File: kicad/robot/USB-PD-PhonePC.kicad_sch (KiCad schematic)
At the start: 42 parts, among them IC1 TPS61253AYFFR, IC4 EFC4626R-TR, U11 MAX77958EWV+T, U15 ESD122DMYR

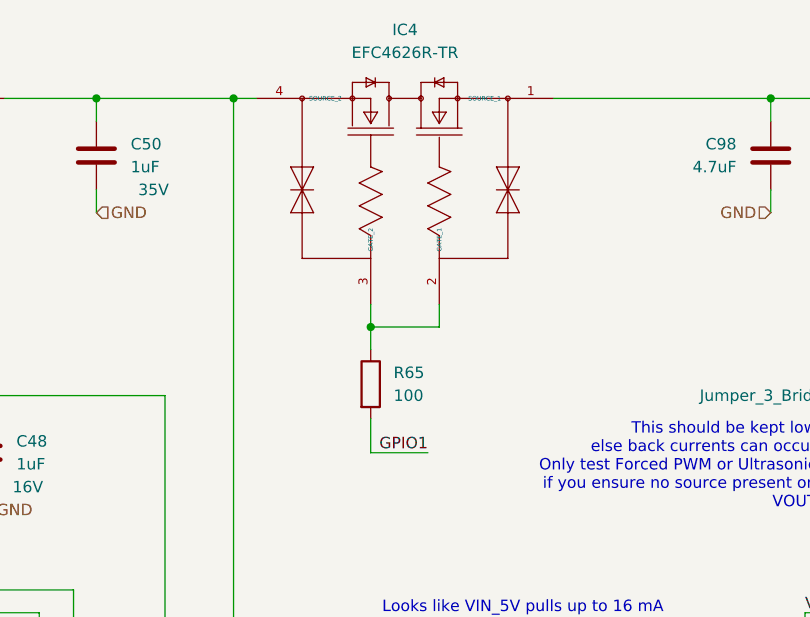
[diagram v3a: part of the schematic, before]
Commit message: Replaced dual mosfet with cheaper pair and common source.
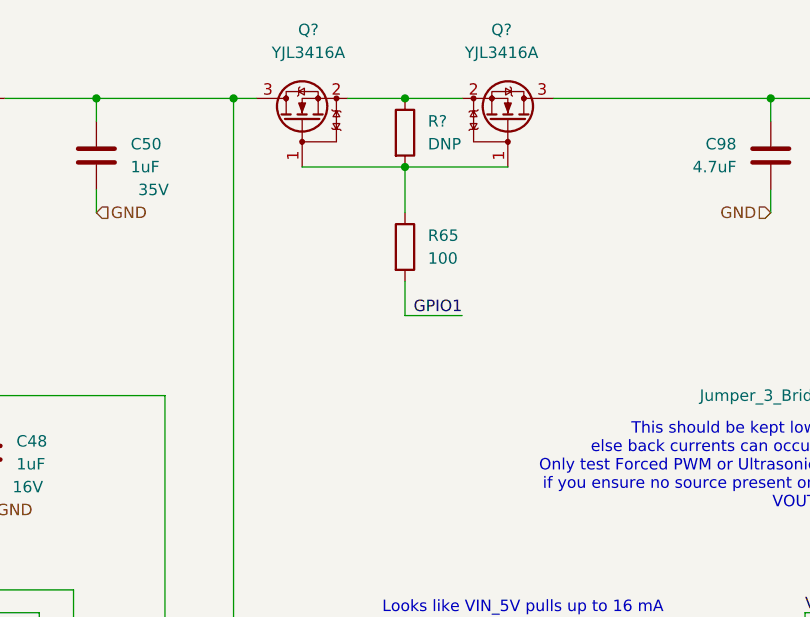
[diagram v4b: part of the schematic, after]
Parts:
- removed IC4: EFC4626R-TR, Package_BGA:ON_SEMI_EFCP1010-4DG-020, symbol Power_Management:EFC4626R-TR
- added Q? (x2): YJL3416A, Package_TO_SOT_SMD:SOT-23, symbol Transistor_FET:YJL3416A
- added R?: DNP, Resistor_SMD:R_0603_1608Metric, symbol Device:R
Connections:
- net at C100.1, C98.1, C99.1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: now also Q?.3 (D)
- net at R65.1: now also Q?.1 (G), Q?.1 (G), R?.2
- net at C50.1, JP4.2 (B), U11.A6 (VBUS): now also Q?.3 (D)
- new net: Q?.2 (S), Q?.2 (S), R?.1
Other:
- moved on the sheet: R65
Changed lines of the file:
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@@
   (junction (at 287.02 293.37) (diameter 0) (color 0 0 0 0)
   )
+  (junction (at 267.97 128.27) (diameter 0) (color 0 0 0 0)
+  )
   (junction (at 322.58 120.65) (diameter 0) (color 0 0 0 0)
   )
@@
   (junction (at 331.47 246.38) (diameter 0) (color 0 0 0 0)
   )
-  (junction (at 264.16 146.05) (diameter 0) (color 0 0 0 0)
-  )
   (junction (at 339.09 234.95) (diameter 0) (color 0 0 0 0)
   )
@@
   )
   (junction (at 236.22 267.97) (diameter 0) (color 0 0 0 0)
+  )
+  (junction (at 267.97 120.65) (diameter 0) (color 0 0 0 0)
   )
   (junction (at 187.96 201.93) (diameter 0) (color 0 0 0 0)
@@
     (stroke (width 0) (type default) (color 0 0 0 0))
   )
-  (wire (pts (xy 264.16 156.21) (xy 264.16 160.02))
+  (wire (pts (xy 267.97 140.97) (xy 267.97 144.78))
     (stroke (width 0) (type default) (color 0 0 0 0))
   )
@@
     (stroke (width 0) (type default) (color 0 0 0 0))
   )
-  (wire (pts (xy 264.16 160.02) (xy 270.51 160.02))
+  (wire (pts (xy 267.97 144.78) (xy 274.32 144.78))
     (stroke (width 0) (type default) (color 0 0 0 0))
   )
@@
     (stroke (width 0) (type default) (color 0 0 0 0))
   )
+  (wire (pts (xy 261.62 120.65) (xy 267.97 120.65))
+    (stroke (width 0) (type default) (color 0 0 0 0))
+  )
   (wire (pts (xy 309.88 254) (xy 316.23 254))
     (stroke (width 0) (type default) (color 0 0 0 0))
@@
     (stroke (width 0) (type default) (color 0 0 0 0))
   )
-  (wire (pts (xy 271.78 143.51) (xy 271.78 146.05))
-    (stroke (width 0) (type default) (color 0 0 0 0))
-  )
   (wire (pts (xy 227.33 215.9) (xy 264.16 215.9))
     (stroke (width 0) (type default) (color 0 0 0 0))
@@
     (stroke (width 0) (type default) (color 0 0 0 0))
   )
-  (wire (pts (xy 264.16 146.05) (xy 264.16 143.51))
+  (wire (pts (xy 267.97 128.27) (xy 267.97 133.35))
     (stroke (width 0) (type default) (color 0 0 0 0))
   )
@@
     (stroke (width 0) (type default) (color 0 0 0 0))
   )
+  (wire (pts (xy 256.54 128.27) (xy 267.97 128.27))
+    (stroke (width 0) (type default) (color 0 0 0 0))
+  )
   (wire (pts (xy 379.73 120.65) (xy 375.92 120.65))
     (stroke (width 0) (type default) (color 0 0 0 0))
@@
     (stroke (width 0) (type default) (color 0 0 0 0))
   )
-  (wire (pts (xy 264.16 148.59) (xy 264.16 146.05))
-    (stroke (width 0) (type default) (color 0 0 0 0))
-  )
   (wire (pts (xy 339.09 269.24) (xy 339.09 264.16))
     (stroke (width 0) (type default) (color 0 0 0 0))
@@
     (stroke (width 0) (type default) (color 0 0 0 0))
   )
-  (wire (pts (xy 271.78 146.05) (xy 264.16 146.05))
-    (stroke (width 0) (type default) (color 0 0 0 0))
-  )
   (wire (pts (xy 309.88 218.44) (xy 317.5 218.44))
     (stroke (width 0) (type default) (color 0 0 0 0))
@@
     (stroke (width 0) (type default) (color 0 0 0 0))
   )
+  (wire (pts (xy 267.97 128.27) (xy 279.4 128.27))
+    (stroke (width 0) (type default) (color 0 0 0 0))
+  )
   (wire (pts (xy 200.66 120.65) (xy 213.36 120.65))
     (stroke (width 0) (type default) (color 0 0 0 0))
@@
   )
   (wire (pts (xy 242.57 267.97) (xy 236.22 267.97))
+    (stroke (width 0) (type default) (color 0 0 0 0))
+  )
+  (wire (pts (xy 267.97 120.65) (xy 274.32 120.65))
     (stroke (width 0) (type default) (color 0 0 0 0))
   )
@@
     (effects (font (size 1.27 1.27)) (justify right bottom))
   )
-  (label "GPIO1" (at 270.51 160.02 180)
+  (label "GPIO1" (at 274.32 144.78 180)
     (effects (font (size 1.27 1.27)) (justify right bottom))
   )
@@
     (pin "2")
   )
+  (symbol (lib_id "Transistor_FET:YJL3416A") (at 279.4 123.19 270) (mirror x) (unit 1)
+    (in_bom yes) (on_board yes) (fields_autoplaced)
+    (property "Reference" "Q?" (id 0) (at 278.7015 113.03 90))
+    (property "Value" "YJL3416A" (id 1) (at 278.7015 115.57 90))
+    (property "Footprint" "Package_TO_SOT_SMD:SOT-23" (id 2) (at 277.495 118.11 0)
+      (effects (font (size 1.27 1.27)) (justify left) hide)
+    )
+    (property "Datasheet" "https://www.21yangjie.com/style/pdf/low-voltage-mosfet/YJL3416A.pdf" (id 3) (at 279.4 123.19 0)
+      (effects (font (size 1.27 1.27)) hide)
+    )
+    (pin "1")
+    (pin "2")
+    (pin "3")
+  )
   (symbol (lib_id "Jumper:Jumper_2_Bridged") (at 177.8 201.93 0) (unit 1)
     (in_bom yes) (on_board yes) (fields_autoplaced)
@@
     (pin "1")
   )
+  (symbol (lib_id "Transistor_FET:YJL3416A") (at 256.54 123.19 90) (unit 1)
+    (in_bom yes) (on_board yes) (fields_autoplaced)
+    (property "Reference" "Q?" (id 0) (at 257.2385 113.03 90))
+    (property "Value" "YJL3416A" (id 1) (at 257.2385 115.57 90))
+    (property "Footprint" "Package_TO_SOT_SMD:SOT-23" (id 2) (at 258.445 118.11 0)
+      (effects (font (size 1.27 1.27)) (justify left) hide)
+    )
+    (property "Datasheet" "https://www.21yangjie.com/style/pdf/low-voltage-mosfet/YJL3416A.pdf" (id 3) (at 256.54 123.19 0)
+      (effects (font (size 1.27 1.27)) hide)
+    )
+    (pin "1")
+    (pin "2")
+    (pin "3")
+  )
   (symbol (lib_id "Device:R") (at 353.06 287.02 0) (unit 1)
     (in_bom yes) (on_board yes) (fields_autoplaced)
@@
     (pin "2")
   )
-  (symbol (lib_id "Power_Management:EFC4626R-TR") (at 267.97 130.81 90) (unit 1)
-    (in_bom yes) (on_board yes) (fields_autoplaced)
-    (property "Reference" "IC4" (id 0) (at 267.97 113.03 90))
-    (property "Value" "EFC4626R-TR" (id 1) (at 267.97 115.57 90))
-    (property "Footprint" "Package_BGA:ON_SEMI_EFCP1010-4DG-020" (id 2) (at 225.425 140.335 0)
-      (effects (font (size 1.27 1.27)) (justify left) hide)
-    )
-    (property "Datasheet" "http://www.onsemi.com/pub/Collateral/ENA2292-D.PDF" (id 3) (at 227.965 140.335 0)
-      (effects (font (size 1.27 1.27)) (justify left) hide)
-    )
-    (property "Description" "MOSFET NCH+NCH 2.5V DRIVE" (id 4) (at 230.505 140.335 0)
-      (effects (font (size 1.27 1.27)) (justify left) hide)
-    )
-    (property "Height" "0.22" (id 5) (at 233.045 140.335 0)
-      (effects (font (size 1.27 1.27)) (justify left) hide)
-    )
-    (property "Manufacturer_Name" "onsemi" (id 6) (at 235.585 140.335 0)
-      (effects (font (size 1.27 1.27)) (justify left) hide)
-    )
-    (property "Manufacturer_Part_Number" "EFC4626R-TR" (id 7) (at 238.125 140.335 0)
-      (effects (font (size 1.27 1.27)) (justify left) hide)
-    )
-    (property "Mouser Part Number" "863-EFC4626R-TR" (id 8) (at 240.665 140.335 0)
-      (effects (font (size 1.27 1.27)) (justify left) hide)
-    )
-    (property "Mouser Price/Stock" "https://www.mouser.com/Search/Refine.aspx?Keyword=863-EFC4626R-TR" (id 9) (at 243.205 140.335 0)
-      (effects (font (size 1.27 1.27)) (justify left) hide)
-    )
-    (property "Arrow Part Number" "" (id 10) (at 245.745 140.335 0)
-      (effects (font (size 1.27 1.27)) (justify left) hide)
-    )
-    (property "Arrow Price/Stock" "" (id 11) (at 248.285 140.335 0)
-      (effects (font (size 1.27 1.27)) (justify left) hide)
-    )
-    (property "Mouser Testing Part Number" "" (id 12) (at 250.825 140.335 0)
-      (effects (font (size 1.27 1.27)) (justify left) hide)
-    )
-    (property "Mouser Testing Price/Stock" "" (id 13) (at 293.37 99.06 0)
-      (effects (font (size 1.27 1.27)) (justify left) hide)
-    )
-    (pin "1")
-    (pin "2")
-    (pin "3")
-    (pin "4")
+  (symbol (lib_id "Device:R") (at 267.97 124.46 0) (unit 1)
+    (in_bom yes) (on_board yes) (fields_autoplaced)
+    (property "Reference" "R?" (id 0) (at 270.51 123.1899 0)
+      (effects (font (size 1.27 1.27)) (justify left))
+    )
+    (property "Value" "DNP" (id 1) (at 270.51 125.7299 0)
+      (effects (font (size 1.27 1.27)) (justify left))
+    )
+    (property "Footprint" "Resistor_SMD:R_0603_1608Metric" (id 2) (at 266.192 124.46 90)
+      (effects (font (size 1.27 1.27)) hide)
+    )
+    (property "Datasheet" "~" (id 3) (at 267.97 124.46 0)
+      (effects (font (size 1.27 1.27)) hide)
+    )
+    (pin "1")
+    (pin "2")
   )
   (symbol (lib_id "Device:C") (at 231.14 259.08 0) (unit 1)
@@
     (pin "2")
   )
-  (symbol (lib_id "Device:R") (at 264.16 152.4 0) (unit 1)
-    (in_bom yes) (on_board yes) (fields_autoplaced)
-    (property "Reference" "R65" (id 0) (at 266.7 151.1299 0)
-      (effects (font (size 1.27 1.27)) (justify left))
-    )
-    (property "Value" "100" (id 1) (at 266.7 153.6699 0)
-      (effects (font (size 1.27 1.27)) (justify left))
-    )
-    (property "Footprint" "Resistor_SMD:R_0603_1608Metric" (id 2) (at 262.382 152.4 90)
-      (effects (font (size 1.27 1.27)) hide)
-    )
-    (property "Datasheet" "~" (id 3) (at 264.16 152.4 0)
-      (effects (font (size 1.27 1.27)) hide)
-    )
+  (symbol (lib_id "Device:R") (at 267.97 137.16 0) (unit 1)
+    (in_bom yes) (on_board yes) (fields_autoplaced)
+    (property "Reference" "R65" (id 0) (at 270.51 135.8899 0)
+      (effects (font (size 1.27 1.27)) (justify left))
+    )
+    (property "Value" "100" (id 1) (at 270.51 138.4299 0)
+      (effects (font (size 1.27 1.27)) (justify left))
+    )
+    (property "Footprint" "Resistor_SMD:R_0603_1608Metric" (id 2) (at 266.192 137.16 90)
+      (effects (font (size 1.27 1.27)) hide)
+    )
+    (property "Datasheet" "~" (id 3) (at 267.97 137.16 0)
+      (effects (font (size 1.27 1.27)) hide)
+    )
